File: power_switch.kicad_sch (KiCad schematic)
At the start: 14 parts, among them Q1 NMOS, Q2 NMOS, Q3 NMOS

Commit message: feat: added power switch schematics
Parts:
- removed C2: C, symbol Device:C
- removed C3: 1nF, symbol Device:C_Small
- removed D1: 5.0, symbol Device:D_Zener
- removed Q1, Q2, Q3: NMOS, symbol Simulation_SPICE:NMOS
- removed R6: R, symbol Device:R
- removed U1: ~, symbol symbols:LM5069
- added C?: 0.1uF, 100V, symbol Device:C_Small
- added Ct: 1nF, symbol Device:C_Small
- added D1: SMF48A, Package_SON:WSON-6-1EP_2x2mm_P0.65mm_EP1x1.6mm_ThermalVias, symbol Diode:SMF48A
- added J1: XT90PW-M, XT90PW-M:AMASS_XT90PW-M, symbol xt90:XT90PW-M
- added Q1, Q2, Q3, Q4, Q5: PSMN3R7-100BSEJ, PSMN3R7-100BSEJ:TRANS_PSMN3R7-100BSEJ, symbol PSMN3R7-100BSEJ:PSMN3R7-100BSEJ
- added R1: 10R, symbol Device:R_Small
- added R2: 1kR, symbol Device:R_Small
- added U?: ~, symbol symbols:_TPS2490
- C1: value 0.01uF -> 27nF, 100V
- R1: value 150kR -> 212kR
- R2: value 11.5kR -> 10kR
- R3: value 95.3kR -> 100kR
- R4: value 3.74kR -> 18kR
- Rs: value 0.1mR -> 0.2mR, 15W
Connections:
- net +48V: now also C?.1, D1.1 (A1), J1.P (POS), U?. (pg); no longer C1.1, R3.1
- net GND: now also C?.2, Ct.2, D1.2 (A2), J1.N (NEG), U?. (pg)
- net at Rs.2: now also Q1.MB, Q2.MB, Q3.MB, Q4.MB, Q5.MB, U?. (pg)
- net SWITCH_HIGH: now reaches R1.2, R2.1
- net at R3.2, R4.1: now also U?. (pg)
- new net: Q1.1, Q2.1, Q3.1, Q4.1, Q5.1, R1.2, R2.1
- new net: C1.1, R2.2
- new net: R1.1, U?. (pg)
- new net: Ct.1, U?. (pg)
- new net: R3.1, U?. (pg)
- new net SWITCH_LOW: U?. (pg)
- new net V_switched: Q1.3, Q2.3, Q3.3, Q4.3, Q5.3, U?. (pg)

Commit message: fix nets
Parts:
- gave numbers to parts that had none: 2
- renumbered Ct to Ct1, Rs to Rs1
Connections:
- net gate_line: now reaches Q1.1, Q2.1, Q3.1, Q4.1, Q5.1, R1.2, R2.1
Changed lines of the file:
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@@
+	)
+	(junction
+		(at 57.15 35.56)
+		(diameter 0)
+		(color 0 0 0 0)
 	)
 	(junction
@@
 	(wire
 		(pts
-			(xy 49.53 35.56) (xy 67.31 35.56)
+			(xy 49.53 35.56) (xy 57.15 35.56)
 		)
 		(stroke
@@
 	(wire
 		(pts
+			(xy 57.15 35.56) (xy 67.31 35.56)
+		)
+		(stroke
+			(width 0)
+			(type default)
+		)
+	)
+	(wire
+		(pts
 			(xy 36.83 35.56) (xy 30.48 35.56)
 		)
@@
 		)
 	)
-	(label "Vcc"
+	(label "gate_line"
+		(at 104.14 34.29 0)
+		(effects
+			(font
+				(size 1.27 1.27)
+			)
+			(justify left bottom)
+		)
+	)
+	(label "battery"
 		(at 40.64 35.56 0)
 		(effects
@@
 		(dnp no)
 		(fields_autoplaced yes)
-		(property "Reference" "Rs"
+		(property "Reference" "Rs1"
 			(at 80.01 26.67 90)
 			(effects
@@
 			(project "power_switch"
 				(path "/81e606bd-bd70-4625-9206-ed6f5fd669d8"
-					(reference "Rs")
+					(reference "Rs1")
 					(unit 1)
 				)
@@
 		(dnp no)
 		(fields_autoplaced yes)
-		(property "Reference" "#PWR?"
+		(property "Reference" "#PWR07"
 			(at 67.31 49.53 0)
 			(effects
@@
 			(project "power_switch"
 				(path "/81e606bd-bd70-4625-9206-ed6f5fd669d8"
-					(reference "#PWR?")
+					(reference "#PWR07")
 					(unit 1)
 				)
@@
 		(dnp no)
 		(fields_autoplaced yes)
-		(property "Reference" "#PWR?"
+		(property "Reference" "#PWR08"
 			(at 87.63 74.93 0)
 			(effects
@@
 			(project "power_switch"
 				(path "/81e606bd-bd70-4625-9206-ed6f5fd669d8"
-					(reference "#PWR?")
+					(reference "#PWR08")
 					(unit 1)
 				)
@@
 		(dnp no)
 		(fields_autoplaced yes)
-		(property "Reference" "#PWR?"
+		(property "Reference" "#PWR03"
 			(at 30.48 64.77 0)
 			(effects
@@
 			(project "power_switch"
 				(path "/81e606bd-bd70-4625-9206-ed6f5fd669d8"
-					(reference "#PWR?")
+					(reference "#PWR03")
 					(unit 1)
 				)
@@
 		(dnp no)
 		(fields_autoplaced yes)
-		(property "Reference" "#PWR?"
+		(property "Reference" "#PWR05"
 			(at 49.53 46.99 0)
 			(effects
@@
 			(project "power_switch"
 				(path "/81e606bd-bd70-4625-9206-ed6f5fd669d8"
-					(reference "#PWR?")
+					(reference "#PWR05")
 					(unit 1)
 				)
@@
 		(dnp no)
 		(fields_autoplaced yes)
-		(property "Reference" "Ct"
+		(property "Reference" "Ct1"
 			(at 90.17 64.7762 0)
 			(effects
@@
 			(project "power_switch"
 				(path "/81e606bd-bd70-4625-9206-ed6f5fd669d8"
-					(reference "Ct")
+					(reference "Ct1")
 					(unit 1)
 				)
@@
 		(dnp no)
 		(fields_autoplaced yes)
-		(property "Reference" "#PWR?"
+		(property "Reference" "#PWR04"
 			(at 36.83 39.37 0)
 			(effects
@@
 			(project "power_switch"
 				(path "/81e606bd-bd70-4625-9206-ed6f5fd669d8"
-					(reference "#PWR?")
+					(reference "#PWR04")
 					(unit 1)
 				)
@@
 				(path "/883cb7fa-3eb5-48d4-9cde-7c11307d94f0/7e8758ce-fdca-4bb6-a847-f546f03772b9"
 					(reference "#PWR04")
+					(unit 1)
+				)
+			)
+		)
+	)
+	(symbol
+		(lib_id "power:PWR_FLAG")
+		(at 57.15 35.56 0)
+		(unit 1)
+		(exclude_from_sim no)
+		(in_bom yes)
+		(on_board yes)
+		(dnp no)
+		(fields_autoplaced yes)
+		(property "Reference" "#FLG01"
+			(at 57.15 33.655 0)
+			(effects
+				(font
+					(size 1.27 1.27)
+				)
+				(hide yes)
+			)
+		)
+		(property "Value" "PWR_FLAG"
+			(at 57.15 30.48 0)
+			(effects
+				(font
+					(size 1.27 1.27)
+				)
+			)
+		)
+		(property "Footprint" ""
+			(at 57.15 35.56 0)
+			(effects
+				(font
+					(size 1.27 1.27)
+				)
+				(hide yes)
+			)
+		)
+		(property "Datasheet" "~"
+			(at 57.15 35.56 0)
+			(effects
+				(font
+					(size 1.27 1.27)
+				)
+				(hide yes)
+			)
+		)
+		(property "Description" "Special symbol for telling ERC where power comes from"
+			(at 57.15 35.56 0)
+			(effects
+				(font
+					(size 1.27 1.27)
+				)
+				(hide yes)
+			)
+		)
+		(pin "1"
+		)
+		(instances
+			(project ""
+				(path "/81e606bd-bd70-4625-9206-ed6f5fd669d8"
+					(reference "#FLG01")
 					(unit 1)
 				)
@@
 		(dnp no)
 		(fields_autoplaced yes)
-		(property "Reference" "C?"
+		(property "Reference" "C2"
 			(at 52.07 36.8362 0)
 			(effects
@@
 			(project "power_switch"
 				(path "/81e606bd-bd70-4625-9206-ed6f5fd669d8"
-					(reference "C?")
+					(reference "C2")
 					(unit 1)
 				)
@@
 		(dnp no)
 		(fields_autoplaced yes)
-		(property "Reference" "U?"
+		(property "Reference" "U1"
 			(at 102.87 47.8946 0)
 			(effects
@@
 			(project "power_switch"
 				(path "/81e606bd-bd70-4625-9206-ed6f5fd669d8"
-					(reference "U?")
+					(reference "U1")
 					(unit 1)
 				)
@@
 		(dnp no)
 		(fields_autoplaced yes)
-		(property "Reference" "#PWR?"
+		(property "Reference" "#PWR06"
 			(at 66.04 77.47 0)
 			(effects
@@
 			(project "power_switch"
 				(path "/81e606bd-bd70-4625-9206-ed6f5fd669d8"
-					(reference "#PWR?")
-					(unit 1)
-				)
+					(reference "#PWR06")
+					(unit 1)
+				)

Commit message: cleaned up file structure
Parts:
- C1: renamed from C2; footprint (none) -> Capacitor_SMD:C_1206_3216Metric_Pad1.33x1.80mm_HandSolder
- C2: renamed from C1; footprint (none) -> Capacitor_SMD:C_1206_3216Metric_Pad1.33x1.80mm_HandSolder
- Ct1: footprint (none) -> Capacitor_SMD:C_1206_3216Metric_Pad1.33x1.80mm_HandSolder
- R1, R2, R3, R4: footprint (none) -> Resistor_SMD:R_1206_3216Metric_Pad1.30x1.75mm_HandSolder
- R5: renamed from Rs1; footprint (none) -> Resistor_SMD:R_1206_3216Metric_Pad1.30x1.75mm_HandSolder
- R6: renamed from R1; footprint (none) -> Resistor_SMD:R_1206_3216Metric_Pad1.30x1.75mm_HandSolder
- R7: renamed from R2; footprint (none) -> Resistor_SMD:R_1206_3216Metric_Pad1.30x1.75mm_HandSolder
- U1: value ~ -> TPS2490; footprint (none) -> vssop:DGS10

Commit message: feat: 48-5v buck converter
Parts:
- Ct1: footprint Capacitor_SMD:C_1206_3216Metric_Pad1.33x1.80mm_HandSolder -> Capacitor_SMD:C_0805_2012Metric_Pad1.18x1.45mm_HandSolder
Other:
- company: (none) -> UMass Robotics
- title: (none) -> High Side Power Switch
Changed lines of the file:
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@@
 	(generator_version "9.0")
 	(paper "A4")
+	(title_block
+		(title "High Side Power Switch")
+		(date "2026-02-04")
+		(rev "Rev 2.0.0")
+		(company "UMass Robotics")
+		(comment 4 "Niranjan Mathirajan")
+	)
 	(junction
 		(at 95.25 25.4)
@@
 			)
 		)
-		(property "Footprint" "Capacitor_SMD:C_1206_3216Metric_Pad1.33x1.80mm_HandSolder"
+		(property "Footprint" "Capacitor_SMD:C_0805_2012Metric_Pad1.18x1.45mm_HandSolder"
 			(at 87.63 66.04 0)
 			(effects

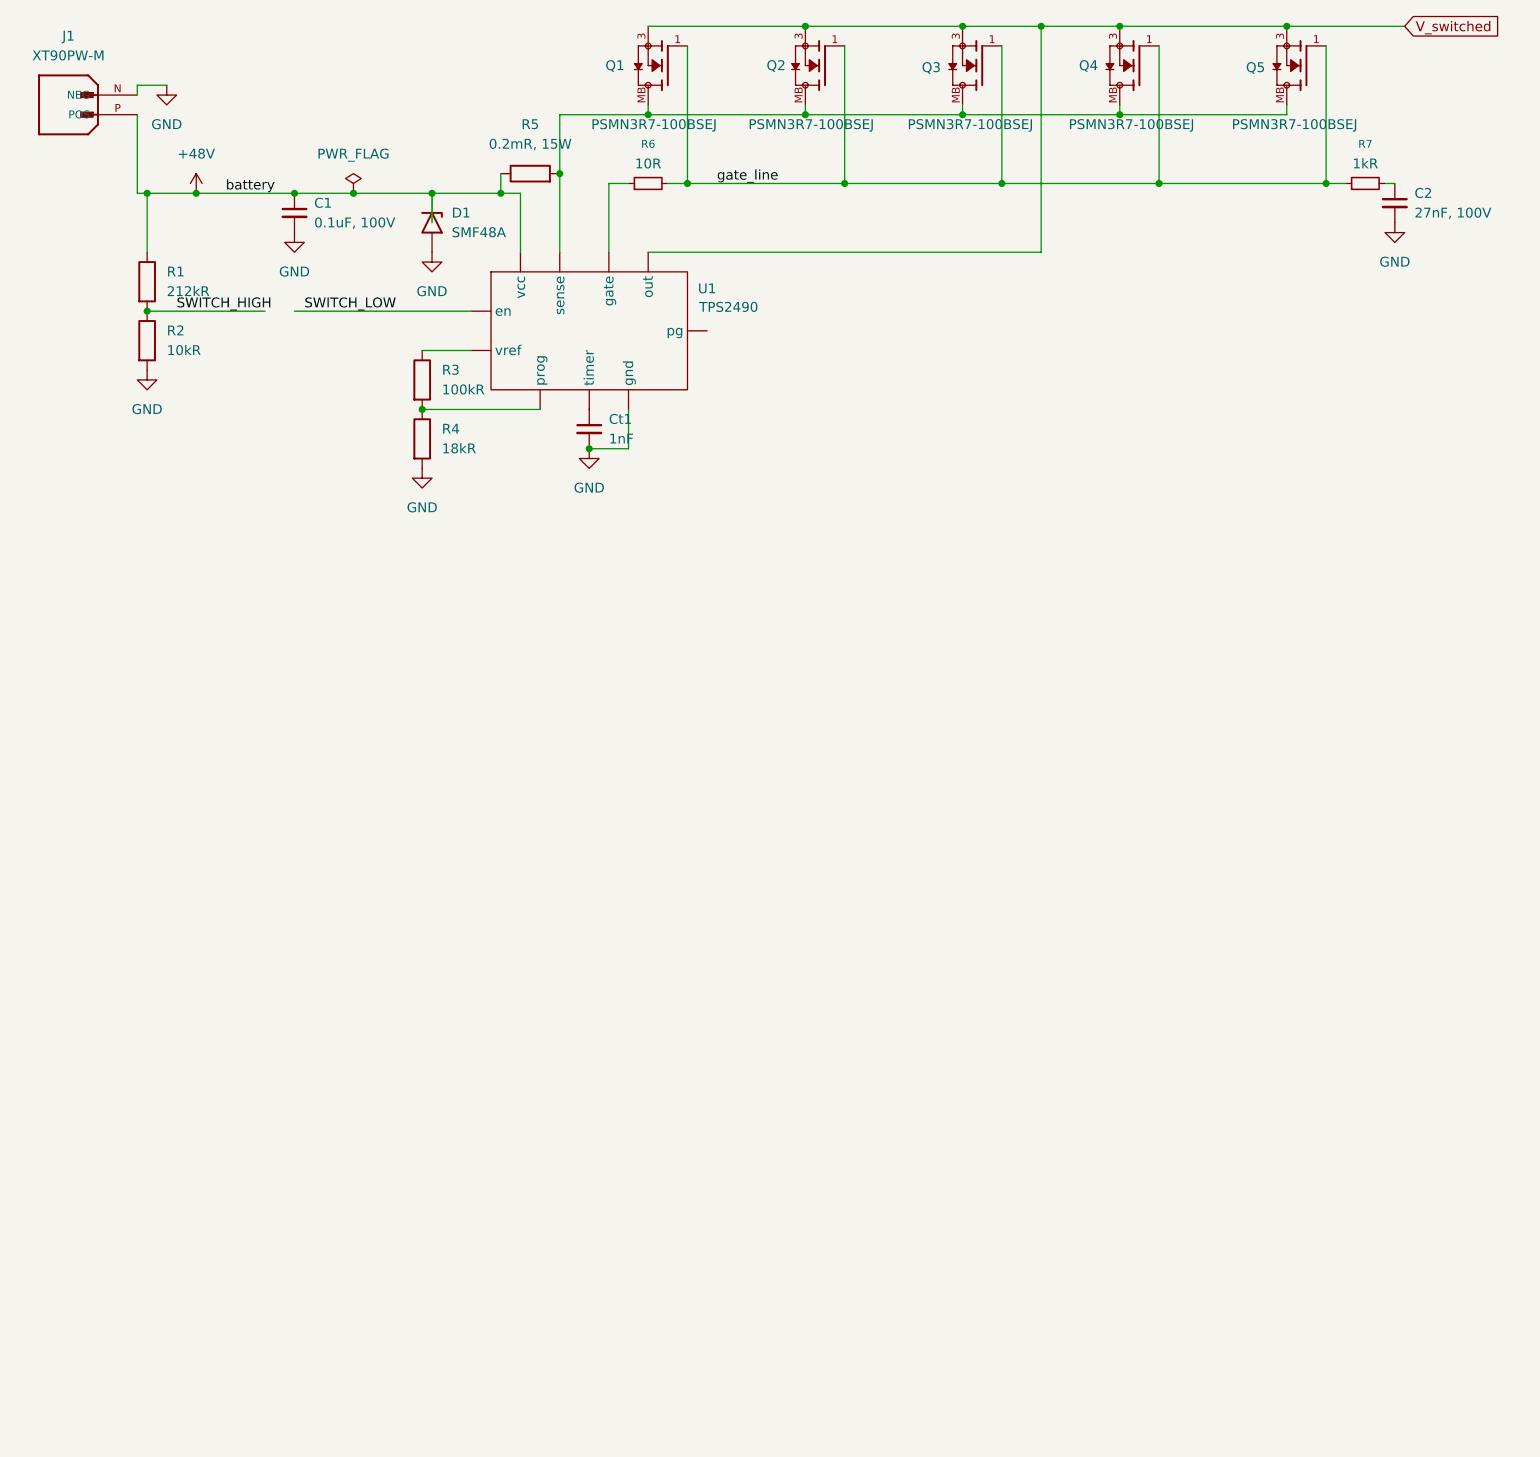
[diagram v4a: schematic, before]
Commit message: fixed ERC errors and footprint for the TPS2490
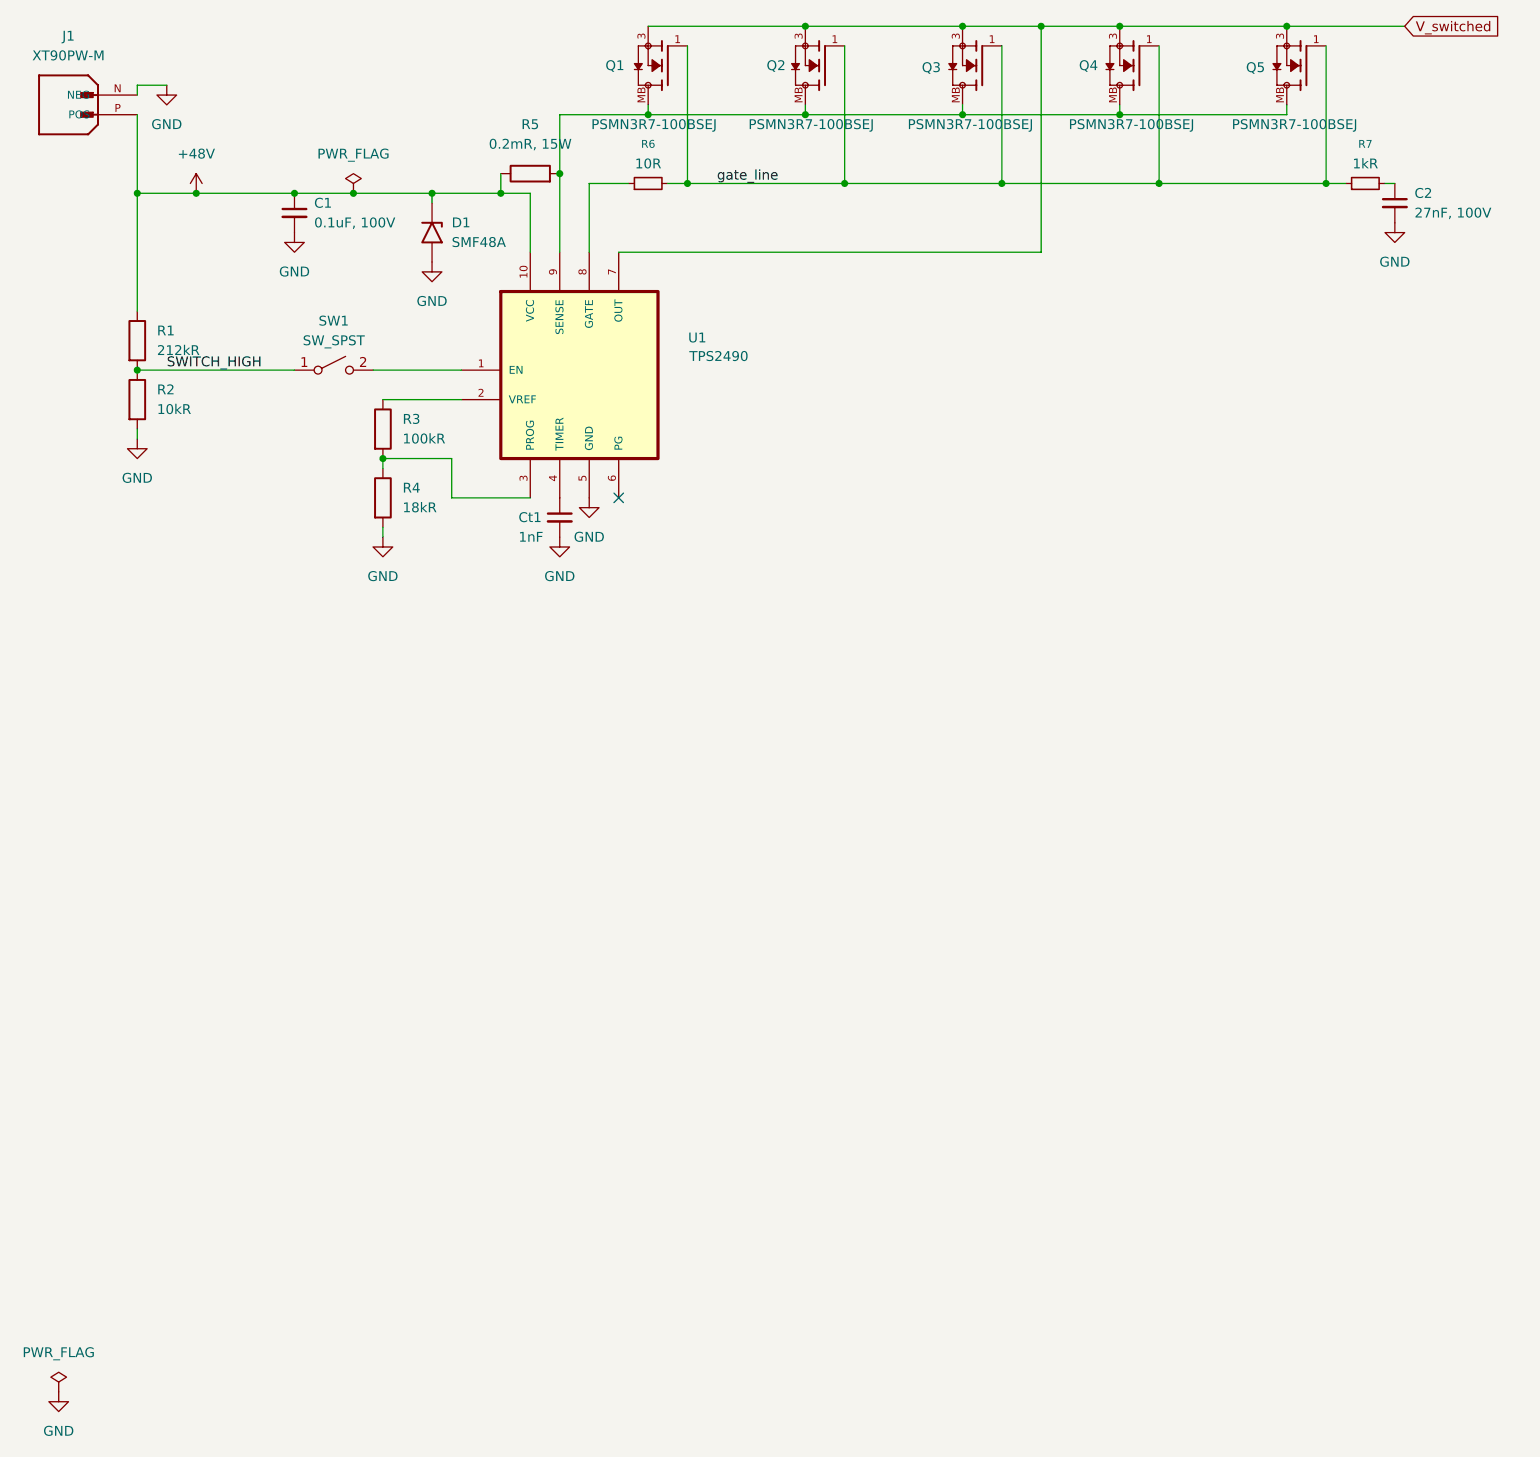
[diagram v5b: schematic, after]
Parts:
- added SW1: SW_SPST, symbol Switch:SW_SPST
- J1: footprint XT90PW-M:AMASS_XT90PW-M -> Connector_AMASS:AMASS_XT90PW-M_1x02_P10.90mm_Horizontal
- Q1, Q2, Q3, Q4, Q5: footprint PSMN3R7-100BSEJ:TRANS_PSMN3R7-100BSEJ -> vssop:D2PAK_NEX
- U1: footprint vssop:DGS10 -> Package_SO:VSSOP-8_3x3mm_P0.65mm; symbol symbols:_TPS2490 -> tps2490g:TPS2490DGSR
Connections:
- net +48V: now also U1.10 (VCC); no longer U1. (pg)
- net GND: now also U1.5 (GND); no longer U1. (pg)
- net SWITCH_HIGH: now also SW1.1 (A)
- net V_switched: now also U1.7 (OUT); no longer U1. (pg)
- net at R3.2, R4.1: now also U1.3 (PROG); no longer U1. (pg)
- net at Q1.MB, Q2.MB, Q3.MB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: now also U1.9 (SENSE); no longer U1. (pg)
- net at R6.1: now also U1.8 (GATE); no longer U1. (pg)
- net at Ct1.1: now also U1.4 (TIMER); no longer U1. (pg)
- net at R3.1: now also U1.2 (VREF); no longer U1. (pg)
- removed net SWITCH_LOW: U1. (pg)
- new net: SW1.2 (B), U1.1 (EN)
- no-connect marks 0 -> 1
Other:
- moved on the sheet: Ct1, D1, R1, R2, R3, R4
